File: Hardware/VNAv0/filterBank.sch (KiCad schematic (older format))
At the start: 18 parts, among them U10 74AHC1G04, U11 PE42440, U12 SN74LVC1G139, U13 PE42440

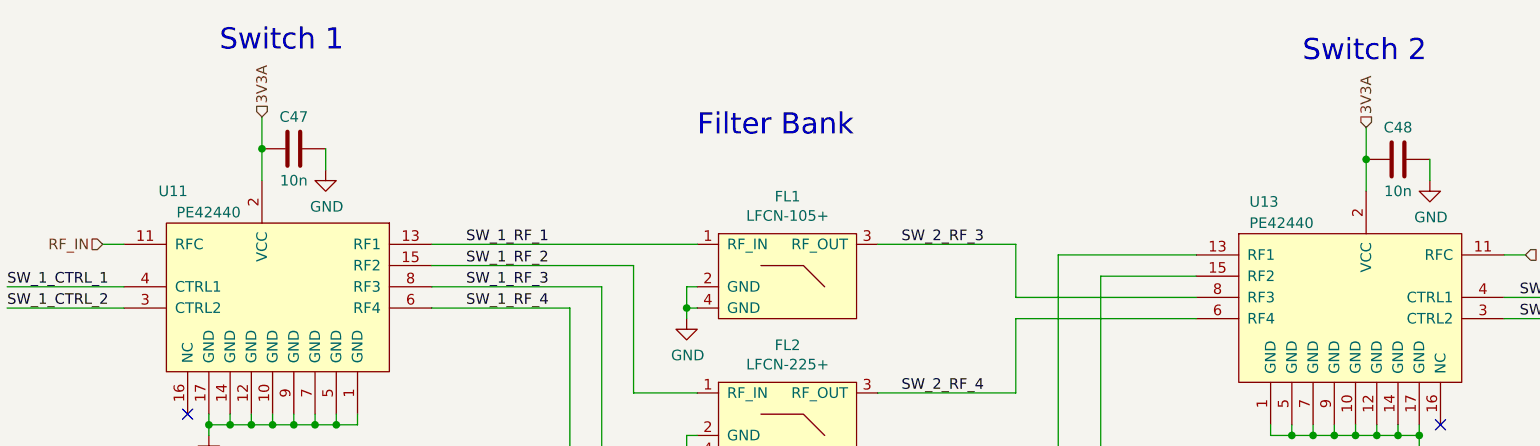
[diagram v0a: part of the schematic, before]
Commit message: tx chain now works, however output power too low
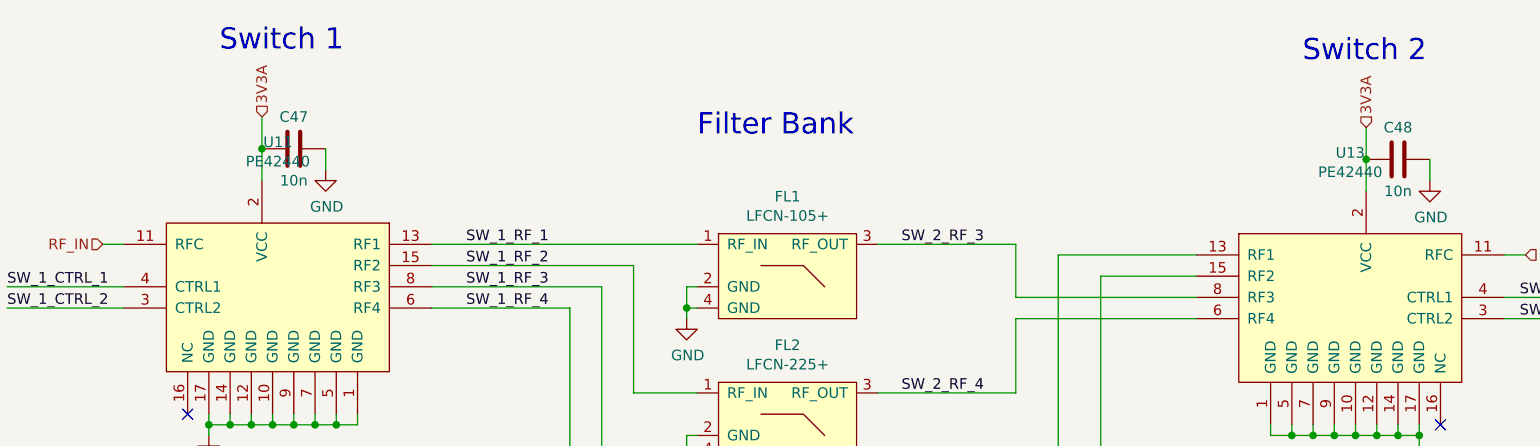
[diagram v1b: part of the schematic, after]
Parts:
- FL1, FL2, FL3, FL4: footprint VNA_Footprints:FV1206 -> (none)
- U10: footprint Package_TO_SOT_SMD:SOT-353_SC-70-5 -> (none)
- U11, U13: footprint VNA_Footprints:QFN-16-1EP_3x3mm_P0.5mm_EP2.7x2.7mm_ThermalVias -> (none)
- U12: footprint Package_SO:VSSOP-8_2.3x2mm_P0.5mm -> (none)
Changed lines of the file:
@@
 Comment4 ""
 $EndDescr
-$Comp
-L VNA_Symbols:PE42440 U13
-U 1 1 5C2A3928
-P 8350 2650
-F 0 "U13" H 7900 3250 50  0000 L CNN
-F 1 "PE42440" H 7900 3150 50  0000 L CNN
-F 2 "VNA_Footprints:QFN-16-1EP_3x3mm_P0.5mm_EP2.7x2.7mm_ThermalVias" H 8050 3150 50  0001 C CNN
-F 3 "" H 8050 3150 50  0001 C CNN
-	1    8350 2650
-	1    0    0    -1
-$EndComp
 Wire Wire Line
 	8000 3100 8000 3150
@@
 Text Label 6650 2950 2    50   ~ 0
 SW_2_RF_4
-$Comp
-L VNA_Symbols:74AHC1G04 U10
-U 1 1 5C2B393D
-P 1900 7050
-F 0 "U10" H 1900 7325 50  0000 C CNN
-F 1 "74AHC1G04" H 1900 7234 50  0000 C CNN
-F 2 "Package_TO_SOT_SMD:SOT-353_SC-70-5" H 1850 7250 50  0001 C CNN
-F 3 "" H 1850 7250 50  0001 C CNN
-	1    1900 7050
-	1    0    0    -1
-$EndComp
 Text Label 3000 6500 2    50   ~ 0
 SW_1_CTRL_1
@@
 Text Label 6700 4400 2    50   ~ 0
 SW_2_RF_2
-$Comp
-L VNA_Symbols:Filter_LFCN FL1
-U 1 1 5C37DE93
-P 5700 2350
-F 0 "FL1" H 5725 2675 50  0000 C CNN
-F 1 "LFCN-105+" H 5725 2584 50  0000 C CNN
-F 2 "VNA_Footprints:FV1206" H 5700 2500 50  0001 C CNN
-F 3 "" H 5700 2500 50  0001 C CNN
-	1    5700 2350
-	1    0    0    -1
-$EndComp
-$Comp
-L VNA_Symbols:Filter_LFCN FL2
-U 1 1 5C3813C7
-P 5700 3050
-F 0 "FL2" H 5725 3375 50  0000 C CNN
-F 1 "LFCN-225+" H 5725 3284 50  0000 C CNN
-F 2 "VNA_Footprints:FV1206" H 5700 3200 50  0001 C CNN
-F 3 "" H 5700 3200 50  0001 C CNN
-	1    5700 3050
-	1    0    0    -1
-$EndComp
-$Comp
-L VNA_Symbols:Filter_LFCN FL3
-U 1 1 5C394D09
-P 5700 3750
-F 0 "FL3" H 5725 4075 50  0000 C CNN
-F 1 "LFCN-400+" H 5725 3984 50  0000 C CNN
-F 2 "VNA_Footprints:FV1206" H 5700 3900 50  0001 C CNN
-F 3 "" H 5700 3900 50  0001 C CNN
-	1    5700 3750
-	1    0    0    -1
-$EndComp
-$Comp
-L VNA_Symbols:Filter_LFCN FL4
-U 1 1 5C3A1E64
-P 5700 4500
-F 0 "FL4" H 5725 4825 50  0000 C CNN
-F 1 "LFCN-1000+" H 5725 4734 50  0000 C CNN
-F 2 "VNA_Footprints:FV1206" H 5700 4650 50  0001 C CNN
-F 3 "" H 5700 4650 50  0001 C CNN
-	1    5700 4500
-	1    0    0    -1
-$EndComp
 Wire Wire Line
 	5300 2450 5250 2450
@@
 Text Label 2050 2450 0    50   ~ 0
 SW_1_CTRL_1
-$Comp
-L VNA_Symbols:PE42440 U11
-U 1 1 5C2A4728
-P 3350 2600
-F 0 "U11" H 3800 3200 50  0000 L CNN
-F 1 "PE42440" H 3550 3100 50  0000 L CNN
-F 2 "VNA_Footprints:QFN-16-1EP_3x3mm_P0.5mm_EP2.7x2.7mm_ThermalVias" H 3050 3100 50  0001 C CNN
-F 3 "" H 3050 3100 50  0001 C CNN
-	1    3350 2600
-	-1   0    0    -1
-$EndComp
 Wire Wire Line
 	9100 2600 9650 2600
@@
 Wire Wire Line
 	2250 6850 2250 7000
-$Comp
-L VNA_Symbols:SN74LVC1G139 U12
-U 1 1 5CE1F9AB
-P 4600 6900
-F 0 "U12" H 4600 7325 50  0000 C CNN
-F 1 "SN74LVC1G139" H 4600 7234 50  0000 C CNN
-F 2 "Package_SO:VSSOP-8_2.3x2mm_P0.5mm" H 4700 7150 100 0001 C CNN
-F 3 "" H 4700 7150 100 0001 C CNN
-	1    4600 6900
-	1    0    0    -1
-$EndComp
 Wire Wire Line
 	4300 6700 4200 6700
@@
 Text Notes 4550 6300 0    100  ~ 0
 LED Filter Indicator
+$Comp
+L VNA_Symbols:PE42440 U11
+U 1 1 5D163069
+P 3350 2600
+F 0 "U11" H 3375 3431 50  0000 C CNN
+F 1 "PE42440" H 3375 3340 50  0000 C CNN
+F 2 "" H 3050 3100 50  0001 C CNN
+F 3 "" H 3050 3100 50  0001 C CNN
+	1    3350 2600
+	-1   0    0    -1
+$EndComp
+$Comp
+L VNA_Symbols:PE42440 U13
+U 1 1 5D1646C5
+P 8350 2650
+F 0 "U13" H 8375 3481 50  0000 C CNN
+F 1 "PE42440" H 8375 3390 50  0000 C CNN
+F 2 "" H 8050 3150 50  0001 C CNN
+F 3 "" H 8050 3150 50  0001 C CNN
+	1    8350 2650
+	1    0    0    -1
+$EndComp
+$Comp
+L VNA_Symbols:Filter_LFCN FL4
+U 1 1 5D166665
+P 5700 4500
+F 0 "FL4" H 5725 4825 50  0000 C CNN
+F 1 "LFCN-1000+" H 5725 4734 50  0000 C CNN
+F 2 "" H 5700 4650 50  0001 C CNN
+F 3 "" H 5700 4650 50  0001 C CNN
+	1    5700 4500
+	1    0    0    -1
+$EndComp
+$Comp
+L VNA_Symbols:Filter_LFCN FL3
+U 1 1 5D167269
+P 5700 3750
+F 0 "FL3" H 5725 4075 50  0000 C CNN
+F 1 "LFCN-400+" H 5725 3984 50  0000 C CNN
+F 2 "" H 5700 3900 50  0001 C CNN
+F 3 "" H 5700 3900 50  0001 C CNN
+	1    5700 3750
+	1    0    0    -1
+$EndComp
+$Comp
+L VNA_Symbols:Filter_LFCN FL2
+U 1 1 5D167516
+P 5700 3050
+F 0 "FL2" H 5725 3375 50  0000 C CNN
+F 1 "LFCN-225+" H 5725 3284 50  0000 C CNN
+F 2 "" H 5700 3200 50  0001 C CNN
+F 3 "" H 5700 3200 50  0001 C CNN
+	1    5700 3050
+	1    0    0    -1
+$EndComp
+$Comp
+L VNA_Symbols:Filter_LFCN FL1
+U 1 1 5D1677E6
+P 5700 2350
+F 0 "FL1" H 5725 2675 50  0000 C CNN
+F 1 "LFCN-105+" H 5725 2584 50  0000 C CNN
+F 2 "" H 5700 2500 50  0001 C CNN
+F 3 "" H 5700 2500 50  0001 C CNN
+	1    5700 2350
+	1    0    0    -1
+$EndComp
+$Comp
+L VNA_Symbols:SN74LVC1G139 U12
+U 1 1 5D169358
+P 4600 6900
+F 0 "U12" H 4600 7325 50  0000 C CNN
+F 1 "SN74LVC1G139" H 4600 7234 50  0000 C CNN
+F 2 "" H 4700 7150 100 0001 C CNN
+F 3 "" H 4700 7150 100 0001 C CNN
+	1    4600 6900
+	1    0    0    -1
+$EndComp
+$Comp
+L VNA_Symbols:74AHC1G04 U10
+U 1 1 5D169DD1
+P 1900 7050
+F 0 "U10" H 1900 7325 50  0000 C CNN
+F 1 "74AHC1G04" H 1900 7234 50  0000 C CNN
+F 2 "" H 1850 7250 50  0001 C CNN
+F 3 "" H 1850 7250 50  0001 C CNN
+	1    1900 7050
+	1    0    0    -1
+$EndComp
 $EndSCHEMATC
